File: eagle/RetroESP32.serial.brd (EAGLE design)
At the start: 71.2 x 115 mm, 70 parts, among them J1 AUDIO_JACK_3.5MM_KIT, J2 SPKR, J3 Batt Conn, J5 503182-1852_503182-1852, J6 USB4110-GF-A_REVB, Q3 DMG3415U-7, Q4 mmbt2222, Q5 mmbt2222, U1 ESP32-WROVER, U3 XC6210B332MR-G, U4 MCP73832T-2ACI/OT, U6 LM4875

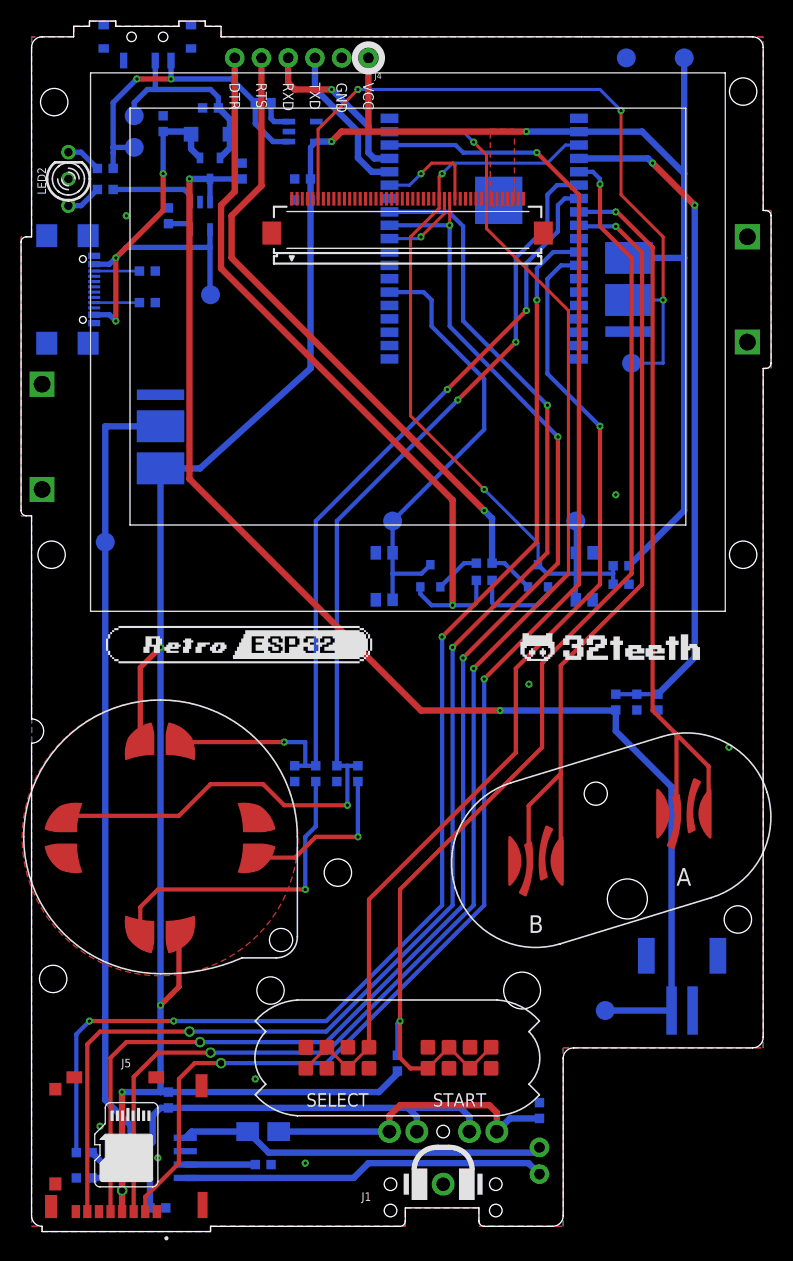
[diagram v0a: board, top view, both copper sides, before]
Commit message: feat: replaced JST with molex connector
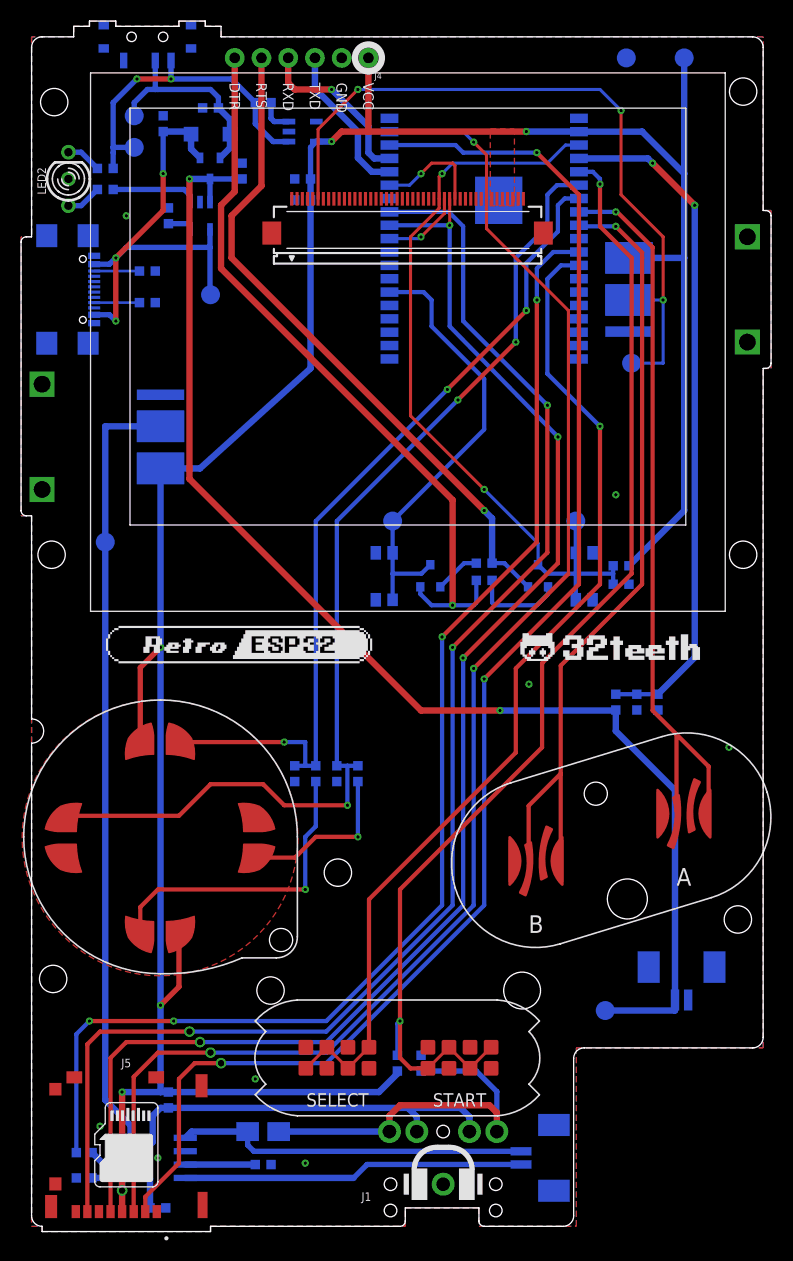
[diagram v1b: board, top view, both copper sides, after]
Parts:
- removed J2: SPKR, RetroESP32:1X02
- removed J3: Batt Conn, RetroESP32:JST-2-SMD
- added X2, X3: 53261-02, con-molex:53261-02
- moved R18 12.1 mm to (37.0, 15.5)
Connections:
- net GND: now also X3.2; no longer J3.1
- net VBAT: now also X3.1; no longer J3.2
- net VOUT1: now also X2.1; no longer J2.1
- net VOUT2: now also X2.2; no longer J2.2
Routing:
- net VIN1: track 29.3 -> 36.5 mm
- net VOUT2: track 34.7 -> 32.4 mm
- net VOUT1: track 34.9 -> 33.7 mm
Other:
- outline, holes or cut-outs redrawn

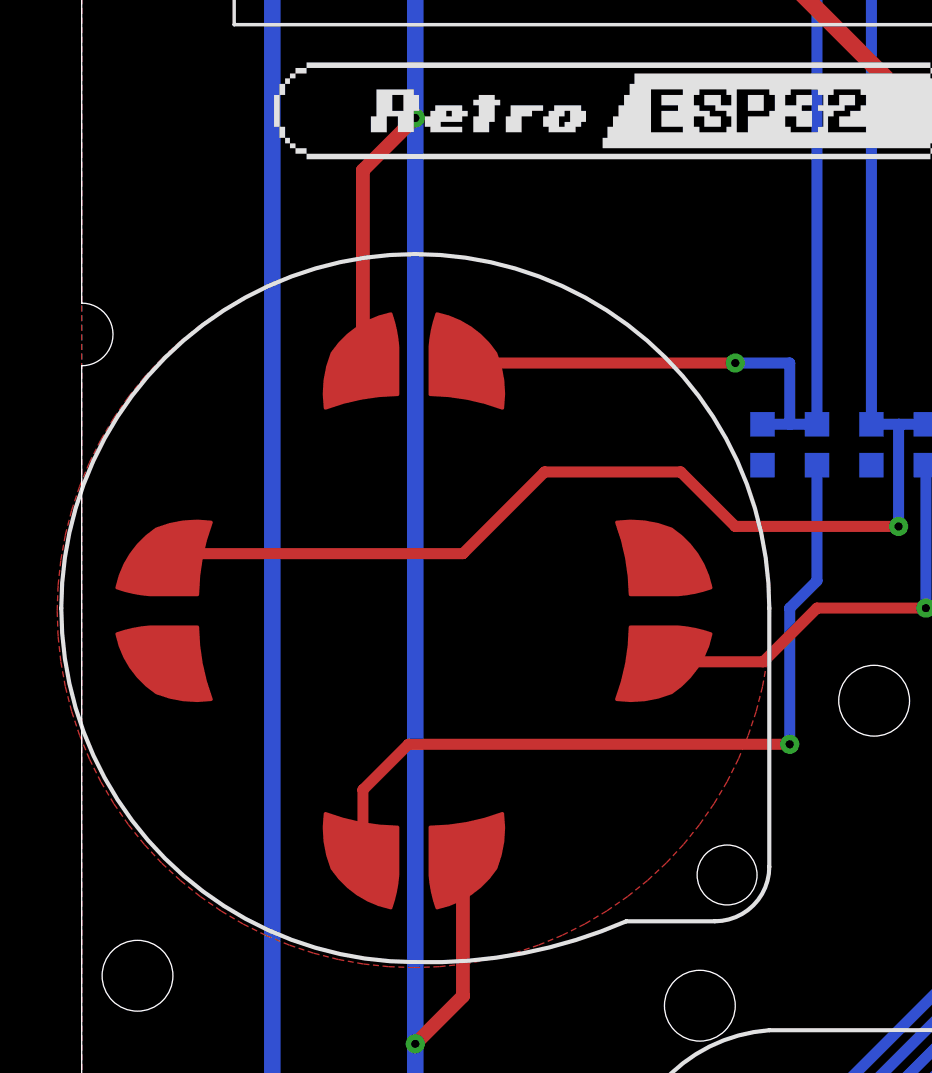
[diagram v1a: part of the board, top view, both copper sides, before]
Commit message: feat: tighter d-pad
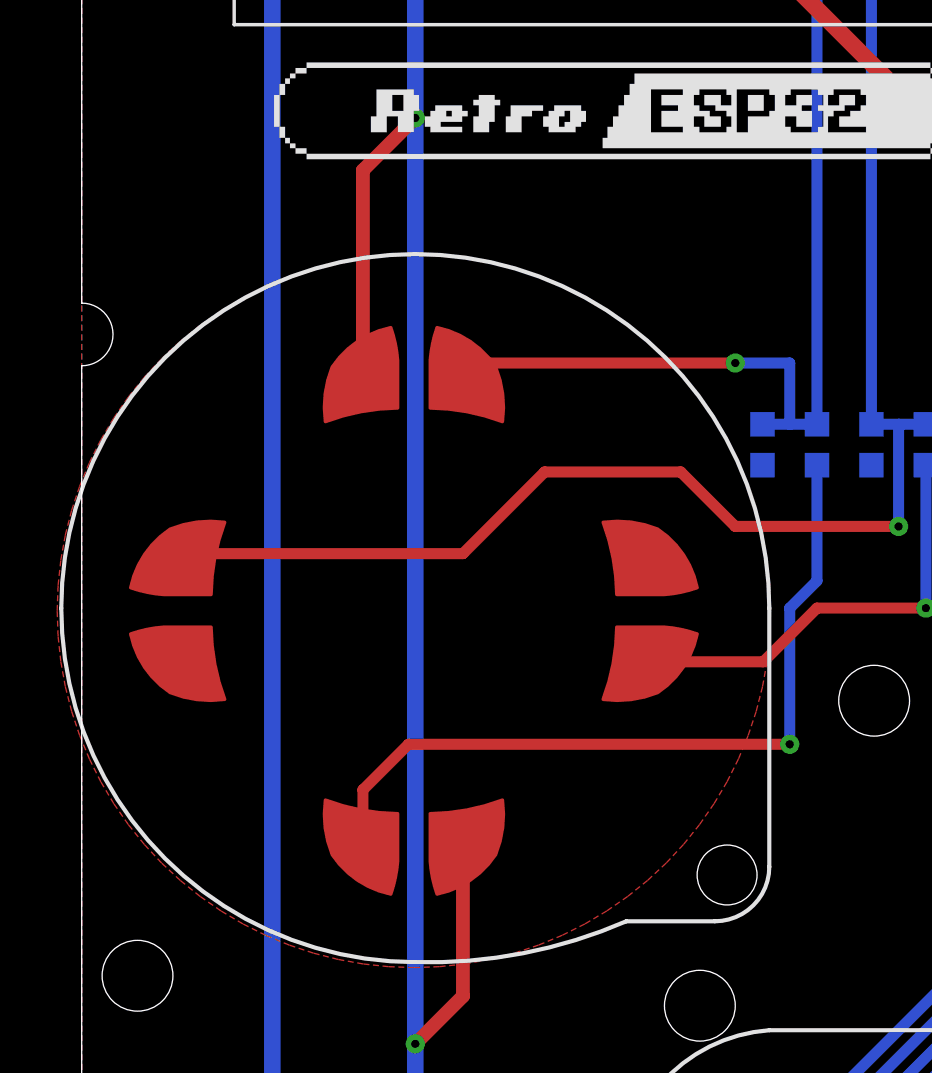
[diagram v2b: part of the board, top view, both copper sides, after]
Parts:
- moved DOWN 0.50 mm to (12.2, 29.7)
- moved LEFT 0.50 mm to (5.00, 36.9)
- moved RIGHT 0.50 mm to (19.4, 36.9)
- moved UP 0.50 mm to (12.2, 44.1)
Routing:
- net RIGHT: track 16.7 -> 17.2 mm
- net DOWN: track 28.7 -> 28.2 mm
- net 3V3: track 269.1 -> 269.6 mm
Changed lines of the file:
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@@
 <drawing>
 <settings>
-<setting alwaysvectorfont="no"/>
+<setting alwaysvectorfont="yes"/>
 <setting verticaltext="up"/>
 </settings>
@@
 <attribute name="IGNORE_BOM" value="TRUE" x="61.97" y="39.2" size="1.778" layer="27" rot="R180" display="off"/>
 </element>
-<element name="UP" library="RetroESP32" library_urn="urn:adsk.eagle:library:12566846" package="DIRECTIONAL-SPACED-PAD" package3d_urn="urn:adsk.eagle:package:40662384/3" value="BUTTONSCONDUCTIVE_BUTTON_DIRECTION_THIN" x="12.2" y="44.6" smashed="yes" rot="R270">
-<attribute name="IGNORE_BOM" value="TRUE" x="12.2" y="44.6" size="1.778" layer="27" rot="R270" display="off"/>
-</element>
-<element name="DOWN" library="RetroESP32" library_urn="urn:adsk.eagle:library:12566846" package="DIRECTIONAL-SPACED-PAD" package3d_urn="urn:adsk.eagle:package:40662384/3" value="BUTTONSCONDUCTIVE_BUTTON_DIRECTION_THIN" x="12.2" y="29.2" smashed="yes" rot="R90">
-<attribute name="IGNORE_BOM" value="TRUE" x="12.2" y="29.2" size="1.778" layer="27" rot="R90" display="off"/>
-</element>
-<element name="LEFT" library="RetroESP32" library_urn="urn:adsk.eagle:library:12566846" package="DIRECTIONAL-SPACED-PAD" package3d_urn="urn:adsk.eagle:package:40662384/3" value="BUTTONSCONDUCTIVE_BUTTON_DIRECTION_THIN" x="4.5" y="36.9" smashed="yes">
-<attribute name="IGNORE_BOM" value="TRUE" x="4.5" y="36.9" size="1.778" layer="27" display="off"/>
-</element>
-<element name="RIGHT" library="RetroESP32" library_urn="urn:adsk.eagle:library:12566846" package="DIRECTIONAL-SPACED-PAD" package3d_urn="urn:adsk.eagle:package:40662384/3" value="BUTTONSCONDUCTIVE_BUTTON_DIRECTION_THIN" x="19.9" y="36.9" smashed="yes" rot="R180">
-<attribute name="IGNORE_BOM" value="TRUE" x="19.9" y="36.9" size="1.778" layer="27" rot="R180" display="off"/>
+<element name="UP" library="RetroESP32" library_urn="urn:adsk.eagle:library:12566846" package="DIRECTIONAL-SPACED-PAD" package3d_urn="urn:adsk.eagle:package:40662384/3" value="BUTTONSCONDUCTIVE_BUTTON_DIRECTION_THIN" x="12.2" y="44.1" smashed="yes" rot="R270">
+<attribute name="IGNORE_BOM" value="TRUE" x="12.2" y="44.1" size="1.778" layer="27" rot="R270" display="off"/>
+</element>
+<element name="DOWN" library="RetroESP32" library_urn="urn:adsk.eagle:library:12566846" package="DIRECTIONAL-SPACED-PAD" package3d_urn="urn:adsk.eagle:package:40662384/3" value="BUTTONSCONDUCTIVE_BUTTON_DIRECTION_THIN" x="12.2" y="29.7" smashed="yes" rot="R90">
+<attribute name="IGNORE_BOM" value="TRUE" x="12.2" y="29.7" size="1.778" layer="27" rot="R90" display="off"/>
+</element>
+<element name="LEFT" library="RetroESP32" library_urn="urn:adsk.eagle:library:12566846" package="DIRECTIONAL-SPACED-PAD" package3d_urn="urn:adsk.eagle:package:40662384/3" value="BUTTONSCONDUCTIVE_BUTTON_DIRECTION_THIN" x="5" y="36.9" smashed="yes">
+<attribute name="IGNORE_BOM" value="TRUE" x="5" y="36.9" size="1.778" layer="27" display="off"/>
+</element>
+<element name="RIGHT" library="RetroESP32" library_urn="urn:adsk.eagle:library:12566846" package="DIRECTIONAL-SPACED-PAD" package3d_urn="urn:adsk.eagle:package:40662384/3" value="BUTTONSCONDUCTIVE_BUTTON_DIRECTION_THIN" x="19.4" y="36.9" smashed="yes" rot="R180">
+<attribute name="IGNORE_BOM" value="TRUE" x="19.4" y="36.9" size="1.778" layer="27" rot="R180" display="off"/>
 </element>
 <element name="R11" library="RetroESP32" library_urn="urn:adsk.eagle:library:12566846" package="0603-MINI" package3d_urn="urn:adsk.eagle:package:12566926/2" override_package3d_urn="urn:adsk.eagle:package:12547731/2" override_package_urn="urn:adsk.eagle:footprint:12547732/1" override_locally_modified="yes" value="10K" x="34.75" y="15.5" smashed="yes" rot="MR90">
@@
 <via x="12.25" y="55" extent="1-16" drill="0.3"/>
 <wire x1="12.25" y1="55" x2="10.327" y2="53.077" width="0.508" layer="1"/>
-<wire x1="10.327" y1="53.077" x2="10.327" y2="45.1" width="0.508" layer="1"/>
+<wire x1="10.327" y1="53.077" x2="10.327" y2="44.6" width="0.508" layer="1"/>
 <wire x1="14" y1="22.75" x2="12.25" y2="21" width="0.508" layer="1"/>
 <polygon width="0" layer="1" thermals="no">
@@
 <vertex x="45.87" y="96.95"/>
 </polygon>
-<wire x1="4" y1="35.027" x2="10.327" y2="45.1" width="0" layer="19" extent="1-1"/>
 </signal>
 <signal name="RESET">
@@
 <wire x1="50" y1="94.5" x2="50" y2="97" width="0.4064" layer="16"/>
 <contactref element="U1" pad="IO35"/>
-<wire x1="14.073" y1="45.1" x2="14.973" y2="46" width="0.4064" layer="1"/>
+<wire x1="14.073" y1="44.6" x2="14.973" y2="46" width="0.4064" layer="1"/>
 <wire x1="14.973" y1="46" x2="24" y2="46" width="0.4064" layer="1"/>
 <via x="24" y="46" extent="1-16" drill="0.3"/>
@@
 <wire x1="24" y1="40" x2="22" y2="42" width="0.4064" layer="1"/>
 <wire x1="17" y1="42" x2="22" y2="42" width="0.4064" layer="1"/>
-<wire x1="4" y1="38.773" x2="4.227" y2="39" width="0.4064" layer="1"/>
+<wire x1="4.5" y1="38.773" x2="4.227" y2="39" width="0.4064" layer="1"/>
 <wire x1="14" y1="39" x2="17" y2="42" width="0.4064" layer="1"/>
 <wire x1="4.227" y1="39" x2="14" y2="39" width="0.4064" layer="1"/>
@@
 <contactref element="DOWN" pad="P$ACTIVE"/>
 <contactref element="R12" pad="2"/>
-<wire x1="10.327" y1="28.7" x2="10.327" y2="30.327" width="0.4064" layer="1"/>
+<wire x1="10.327" y1="29.2" x2="10.327" y2="30.327" width="0.4064" layer="1"/>
 <wire x1="12" y1="32" x2="26" y2="32" width="0.4064" layer="1"/>
 <via x="26" y="32" extent="1-16" drill="0.3"/>
@@
 <contactref element="RIGHT" pad="P$ACTIVE"/>
 <contactref element="R14" pad="2"/>
-<wire x1="20.4" y1="35.027" x2="25.027" y2="35.027" width="0.4064" layer="1"/>
+<wire x1="19.9" y1="35.027" x2="25.027" y2="35.027" width="0.4064" layer="1"/>
 <wire x1="25.027" y1="35.027" x2="27" y2="37" width="0.4064" layer="1"/>
 <wire x1="27" y1="37" x2="31" y2="37" width="0.4064" layer="1"/>

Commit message: feat: released X
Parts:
- added D1: LTST-C155GEKT, LTST-C155GEKT:LED_LTST-C155GEKT
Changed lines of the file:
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@@
 </layers>
 <board>
-<fusionsync huburn="a.cGVyc29uYWw6dWUyYjExYjI4" projecturn="a.cGVyc29uYWw6dWUyYjExYjI4IzIwMTkwNjA2MTk3NjIxNDMx" f3durn="urn:adsk.wipprod:dm.lineage:ZWmRsYaBRGKwdBkIFFlMag" pcbguid="" lastpulledtime="" lastsyncedchangeguid="" latestrevisionid="7732cfb7-a4b0-4dd0-aef1-4c9a1b6ed651" lastsyncedrevisionid="f3f9ff4f-a156-4fd5-8441-28e31faf31d2" lastboardhashguid="41d33a08-9d62-a667-3f9b-4f8ad2bc6665" lastpushedtime="2023-03-30T16:58:05Z" linktopcb3d="true"/>
+<fusionsync huburn="a.cGVyc29uYWw6dWUyYjExYjI4" projecturn="a.cGVyc29uYWw6dWUyYjExYjI4IzIwMTkwNjA2MTk3NjIxNDMx" f3durn="urn:adsk.wipprod:dm.lineage:ZWmRsYaBRGKwdBkIFFlMag" pcbguid="" lastpulledtime="" lastsyncedchangeguid="" latestrevisionid="7732cfb7-a4b0-4dd0-aef1-4c9a1b6ed651" lastsyncedrevisionid="f3f9ff4f-a156-4fd5-8441-28e31faf31d2" lastboardhashguid="41d33a08-9d62-a667-3f9b-4f8ad2bc6665" lastpushedtime="2023-03-30T16:58:05Z" linktopcb3d="false"/>
 <fusionteam huburn="a.cGVyc29uYWw6dWUyYjExYjI4" projecturn="a.cGVyc29uYWw6dWUyYjExYjI4IzIwMTkwNjA2MTk3NjIxNDMx" folderUrn="urn:adsk.wipprod:fs.folder:co.pA_OyOrURcuKuaZfHTjB4g" urn="urn:adsk.wipprod:dm.lineage:ZdROvaXvSf-QMBwcavZMUg"  versionUrn="urn:adsk.wipprod:fs.file:vf.ZdROvaXvSf-QMBwcavZMUg?version=3" camFileUrn="urn:adsk.wipprod:dm.lineage:iU1Nsl3HQ2WKUaZAR9U5UA" camFileVersionUrn="urn:adsk.wipprod:fs.file:vf.iU1Nsl3HQ2WKUaZAR9U5UA?version=3" lastpublishedchangeguid="86bd4f74-7e00-3941-ed52-f5fd457b13a9"/>
 <plain>
@@
 <attribute name="VALUE" x="64.375" y="21" size="1.27" layer="28" rot="MR0"/>
 </element>
+<element name="D1" library="LTST-C155GEKT" package="LED_LTST-C155GEKT" value="LTST-C155GEKT" x="3.5" y="99.5" smashed="yes" rot="R90">
+<attribute name="DESCRIPTION" value=" Green, Red 569nm Green, 621nm Red LED Indication - Discrete 2.1V Green, 2V Red 1210 (3225 Metric) " x="3.5" y="99.5" size="1.778" layer="27" rot="R90" display="off"/>
+<attribute name="DIGI-KEY_PART_NUMBER" value="160-1172-2-ND" x="3.5" y="99.5" size="1.778" layer="27" rot="R90" display="off"/>
+<attribute name="MF" value="Lite-On Inc." x="3.5" y="99.5" size="1.778" layer="27" rot="R90" display="off"/>
+<attribute name="MP" value="LTST-C155GEKT" x="3.5" y="99.5" size="1.778" layer="27" rot="R90" display="off"/>
+<attribute name="NAME" x="1.7" y="96.75" size="0.8128" layer="25" rot="R90"/>
+<attribute name="PACKAGE" value="None" x="3.5" y="99.5" size="1.778" layer="27" rot="R90" display="off"/>
+<attribute name="PURCHASE-URL" value="https://pricing.snapeda.com/search?q=LTST-C155GEKT&amp;ref=eda" x="3.5" y="99.5" size="1.778" layer="27" rot="R90" display="off"/>
+<attribute name="VALUE" x="5.3" y="96.75" size="0.8128" layer="27" rot="R90" align="top-left"/>
+</element>
 </elements>

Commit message: update: BOM for X
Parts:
- removed D1: LTST-C155GEKT, LTST-C155GEKT:LED_LTST-C155GEKT
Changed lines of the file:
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@@
 <drawing>
 <settings>
-<setting alwaysvectorfont="yes"/>
+<setting alwaysvectorfont="no"/>
 <setting verticaltext="up"/>
 </settings>
@@
 </layers>
 <board>
-<fusionsync huburn="a.cGVyc29uYWw6dWUyYjExYjI4" projecturn="a.cGVyc29uYWw6dWUyYjExYjI4IzIwMTkwNjA2MTk3NjIxNDMx" f3durn="urn:adsk.wipprod:dm.lineage:ZWmRsYaBRGKwdBkIFFlMag" pcbguid="" lastpulledtime="" lastsyncedchangeguid="" latestrevisionid="7732cfb7-a4b0-4dd0-aef1-4c9a1b6ed651" lastsyncedrevisionid="f3f9ff4f-a156-4fd5-8441-28e31faf31d2" lastboardhashguid="41d33a08-9d62-a667-3f9b-4f8ad2bc6665" lastpushedtime="2023-03-30T16:58:05Z" linktopcb3d="false"/>
+<fusionsync huburn="a.cGVyc29uYWw6dWUyYjExYjI4" projecturn="a.cGVyc29uYWw6dWUyYjExYjI4IzIwMTkwNjA2MTk3NjIxNDMx" f3durn="urn:adsk.wipprod:dm.lineage:ZWmRsYaBRGKwdBkIFFlMag" pcbguid="" lastpulledtime="" lastsyncedchangeguid="" latestrevisionid="7732cfb7-a4b0-4dd0-aef1-4c9a1b6ed651" lastsyncedrevisionid="f3f9ff4f-a156-4fd5-8441-28e31faf31d2" lastboardhashguid="41d33a08-9d62-a667-3f9b-4f8ad2bc6665" lastpushedtime="2023-03-30T16:58:05Z" linktopcb3d="true"/>
 <fusionteam huburn="a.cGVyc29uYWw6dWUyYjExYjI4" projecturn="a.cGVyc29uYWw6dWUyYjExYjI4IzIwMTkwNjA2MTk3NjIxNDMx" folderUrn="urn:adsk.wipprod:fs.folder:co.pA_OyOrURcuKuaZfHTjB4g" urn="urn:adsk.wipprod:dm.lineage:ZdROvaXvSf-QMBwcavZMUg"  versionUrn="urn:adsk.wipprod:fs.file:vf.ZdROvaXvSf-QMBwcavZMUg?version=3" camFileUrn="urn:adsk.wipprod:dm.lineage:iU1Nsl3HQ2WKUaZAR9U5UA" camFileVersionUrn="urn:adsk.wipprod:fs.file:vf.iU1Nsl3HQ2WKUaZAR9U5UA?version=3" lastpublishedchangeguid="86bd4f74-7e00-3941-ed52-f5fd457b13a9"/>
 <plain>
@@
 <attribute name="VALUE" x="64.375" y="21" size="1.27" layer="28" rot="MR0"/>
 </element>
-<element name="D1" library="LTST-C155GEKT" package="LED_LTST-C155GEKT" value="LTST-C155GEKT" x="3.5" y="99.5" smashed="yes" rot="R90">
-<attribute name="DESCRIPTION" value=" Green, Red 569nm Green, 621nm Red LED Indication - Discrete 2.1V Green, 2V Red 1210 (3225 Metric) " x="3.5" y="99.5" size="1.778" layer="27" rot="R90" display="off"/>
-<attribute name="DIGI-KEY_PART_NUMBER" value="160-1172-2-ND" x="3.5" y="99.5" size="1.778" layer="27" rot="R90" display="off"/>
-<attribute name="MF" value="Lite-On Inc." x="3.5" y="99.5" size="1.778" layer="27" rot="R90" display="off"/>
-<attribute name="MP" value="LTST-C155GEKT" x="3.5" y="99.5" size="1.778" layer="27" rot="R90" display="off"/>
-<attribute name="NAME" x="1.7" y="96.75" size="0.8128" layer="25" rot="R90"/>
-<attribute name="PACKAGE" value="None" x="3.5" y="99.5" size="1.778" layer="27" rot="R90" display="off"/>
-<attribute name="PURCHASE-URL" value="https://pricing.snapeda.com/search?q=LTST-C155GEKT&amp;ref=eda" x="3.5" y="99.5" size="1.778" layer="27" rot="R90" display="off"/>
-<attribute name="VALUE" x="5.3" y="96.75" size="0.8128" layer="27" rot="R90" align="top-left"/>
-</element>
 </elements>
